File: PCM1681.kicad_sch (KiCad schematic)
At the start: 37 parts, among them J1 USB_C_Receptacle_PowerOnly_6P, J2 Conn_01x10_Pin, J3 Conn_01x05_Pin, J4 Conn_01x05_Pin, J5 Conn_01x05_Pin, J6 AudioJack3, J7 AudioJack3, J8 AudioJack3, J9 AudioJack3, SW1 SW_DIP_x04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

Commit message: First order
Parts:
- removed J6, J7, J8, J9: AudioJack3, Connector_Audio:Jack_3.5mm_CUI_SJ-3523-SMT_Horizontal, symbol Connector_Audio:AudioJack3
- added J10, J11, J12: AudioJack4, Connector_Audio:Jack_3.5mm_PJ320D_Horizontal, symbol Connector_Audio:AudioJack4
- added J13: \, Connector_Audio:Jack_3.5mm_PJ320D_Horizontal, symbol Connector_Audio:AudioJack4
- C5, C7, C8, C9: LCSC C15195 -> C15195
- J2, J3, J4, J5, U2: now not fitted
- U1: LCSC AMS1117-3.3 C6186 -> C6186
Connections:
- net GNDA: now also J10.S, J11.S, J12.S, J13.S
- net LPF/OUT1: now also J10.T
- net LPF/OUT2: now also J10.R1
- net LPF/OUT3: now also J11.T
- net LPF/OUT4: now also J11.R1
- net LPF1/OUT1: now also J12.T
- net LPF1/OUT2: now also J12.R1
- net LPF1/OUT3: now also J13.T
- net LPF1/OUT4: now also J13.R1
- no-connect marks 0 -> 3

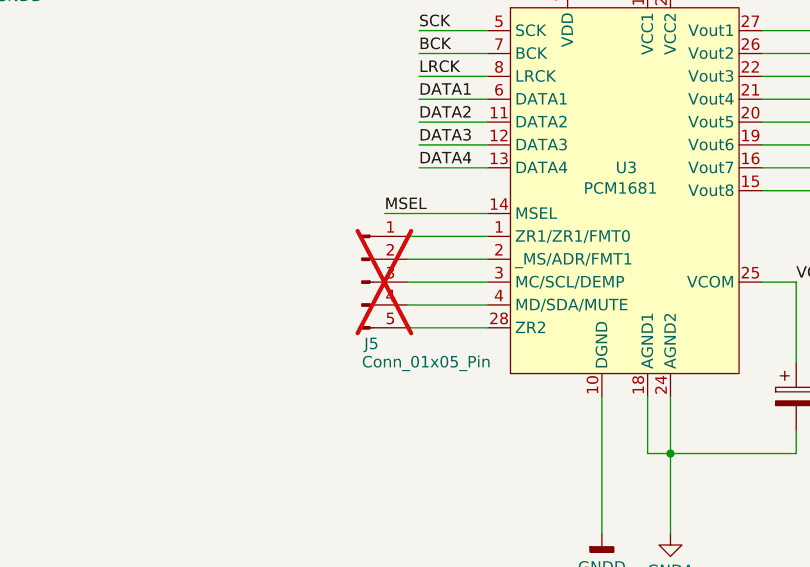
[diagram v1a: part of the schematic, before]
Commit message: Updated LCSC parts number for unmatched footprint
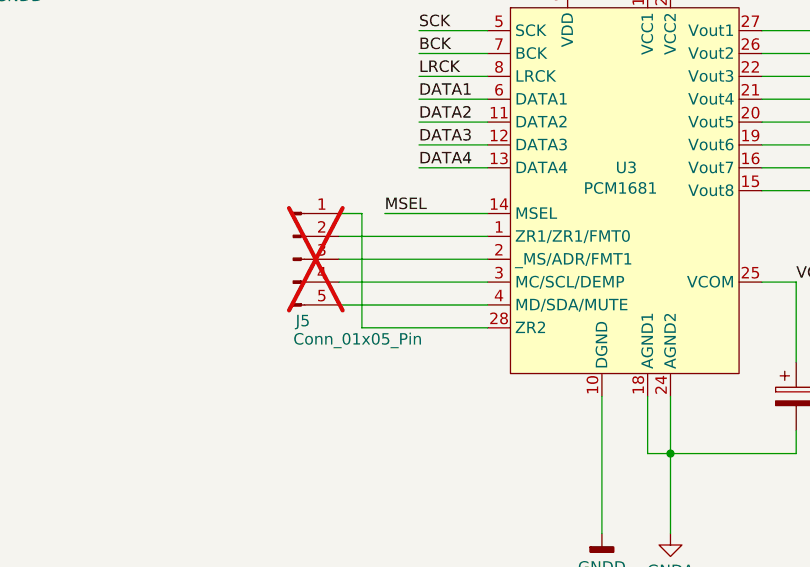
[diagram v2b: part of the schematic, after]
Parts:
- SW1: footprint Button_Switch_SMD:SW_DIP_SPSTx04_Slide_6.7x11.72mm_W6.73mm_P2.54mm_LowProfile_JPin -> Button_Switch_SMD:SW_DIP_SPSTx04_Slide_KingTek_DSHP04TJ_W5.25mm_P1.27mm_JPin; LCSC C6331176 -> C224996
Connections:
- net at U3.1 (ZR1/ZR1/FMT0): now also J5.2 (Pin_2); no longer J5.1 (Pin_1)
- net at U3.2 (_MS/ADR/FMT1): now also J5.3 (Pin_3); no longer J5.2 (Pin_2)
- net at U3.28 (ZR2): now also J5.1 (Pin_1); no longer J5.5 (Pin_5)
- net at U3.3 (MC/SCL/DEMP): now also J5.4 (Pin_4); no longer J5.3 (Pin_3)
- net at U3.4 (MD/SDA/MUTE): now also J5.5 (Pin_5); no longer J5.4 (Pin_4)
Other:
- moved on the sheet: J5
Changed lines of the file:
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@@
 	(wire
 		(pts
-			(xy 170.18 128.27) (xy 179.07 128.27)
-		)
-		(stroke
-			(width 0)
-			(type default)
-		)
-	)
-	(wire
-		(pts
 			(xy 171.45 115.57) (xy 179.07 115.57)
 		)
@@
 	(wire
 		(pts
+			(xy 162.56 128.27) (xy 179.07 128.27)
+		)
+		(stroke
+			(width 0)
+			(type default)
+		)
+	)
+	(wire
+		(pts
 			(xy 184.15 83.82) (xy 187.96 83.82)
 		)
@@
 	(wire
 		(pts
-			(xy 170.18 138.43) (xy 179.07 138.43)
-		)
-		(stroke
-			(width 0)
-			(type default)
-		)
-	)
-	(wire
-		(pts
 			(xy 151.13 86.36) (xy 153.67 86.36)
 		)
@@
 	(wire
 		(pts
+			(xy 162.56 125.73) (xy 165.1 125.73)
+		)
+		(stroke
+			(width 0)
+			(type default)
+		)
+	)
+	(wire
+		(pts
 			(xy 199.39 93.98) (xy 201.93 93.98)
 		)
@@
 	(wire
 		(pts
+			(xy 165.1 138.43) (xy 179.07 138.43)
+		)
+		(stroke
+			(width 0)
+			(type default)
+		)
+	)
+	(wire
+		(pts
 			(xy 83.82 73.66) (xy 83.82 81.28)
 		)
@@
 	(wire
 		(pts
-			(xy 170.18 133.35) (xy 179.07 133.35)
+			(xy 83.82 101.6) (xy 83.82 104.14)
 		)
 		(stroke
@@
 	(wire
 		(pts
-			(xy 83.82 101.6) (xy 83.82 104.14)
+			(xy 162.56 130.81) (xy 179.07 130.81)
 		)
 		(stroke
@@
 	(wire
 		(pts
+			(xy 165.1 125.73) (xy 165.1 138.43)
+		)
+		(stroke
+			(width 0)
+			(type default)
+		)
+	)
+	(wire
+		(pts
 			(xy 62.23 87.63) (xy 62.23 90.17)
 		)
@@
 	(wire
 		(pts
+			(xy 162.56 135.89) (xy 179.07 135.89)
+		)
+		(stroke
+			(width 0)
+			(type default)
+		)
+	)
+	(wire
+		(pts
 			(xy 71.12 73.66) (xy 83.82 73.66)
 		)
@@
 	(wire
 		(pts
-			(xy 170.18 130.81) (xy 179.07 130.81)
-		)
-		(stroke
-			(width 0)
-			(type default)
-		)
-	)
-	(wire
-		(pts
 			(xy 30.48 55.88) (xy 30.48 58.42)
 		)
@@
 	(wire
 		(pts
-			(xy 170.18 135.89) (xy 179.07 135.89)
+			(xy 199.39 152.4) (xy 199.39 161.29)
 		)
 		(stroke
@@
 	(wire
 		(pts
-			(xy 199.39 152.4) (xy 199.39 161.29)
+			(xy 209.55 93.98) (xy 212.09 93.98)
 		)
 		(stroke
@@
 	(wire
 		(pts
-			(xy 209.55 93.98) (xy 212.09 93.98)
+			(xy 162.56 133.35) (xy 179.07 133.35)
 		)
 		(stroke
@@
 			)
 		)
-		(property "Footprint" "Button_Switch_SMD:SW_DIP_SPSTx04_Slide_6.7x11.72mm_W6.73mm_P2.54mm_LowProfile_JPin"
+		(property "Footprint" "Button_Switch_SMD:SW_DIP_SPSTx04_Slide_KingTek_DSHP04TJ_W5.25mm_P1.27mm_JPin"
 			(at 143.51 86.36 0)
 			(effects
@@
 			)
 		)
-		(property "LCSC" "C6331176"
+		(property "LCSC" "C224996"
 			(at 143.51 86.36 0)
 			(effects
@@
 	(symbol
 		(lib_id "Connector:Conn_01x05_Pin")
-		(at 165.1 133.35 0)
+		(at 157.48 130.81 0)
 		(unit 1)
 		(exclude_from_sim no)
@@
 		(dnp yes)
 		(property "Reference" "J5"
-			(at 165.354 140.208 0)
+			(at 157.734 137.668 0)
 			(effects
 				(font
@@
 		)
 		(property "Value" "Conn_01x05_Pin"
-			(at 165.1 142.24 0)
+			(at 157.48 139.7 0)
 			(effects
 				(font
@@
 		)
 		(property "Footprint" "Connector_PinHeader_2.54mm:PinHeader_1x05_P2.54mm_Vertical"
-			(at 165.1 133.35 0)
+			(at 157.48 130.81 0)
 			(effects
 				(font
@@
 		)
 		(property "Datasheet" "~"
-			(at 165.1 133.35 0)
+			(at 157.48 130.81 0)
 			(effects
 				(font
@@
 		)
 		(property "Description" "Generic connector, single row, 01x05, script generated"
-			(at 165.1 133.35 0)
+			(at 157.48 130.81 0)
 			(effects
 				(font
